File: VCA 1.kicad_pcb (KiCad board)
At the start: 2 copper layers, 185.7 x 142.5 mm, 46 parts, among them J1 Eurorack 2x8hs, J10 IN3, J11 IN4, J12 IN5, J13 OUT1, J14 OUT2, J15 OUT3, J16 OUT4, J2 LED 1x2s, J3 IN 1x6s, J4 OUT 1x4s, J5 LED 1x2h, J6 IN 1x6h, J7 OUT 1x4h, J8 IN1, J9 IN2, U1 TL074

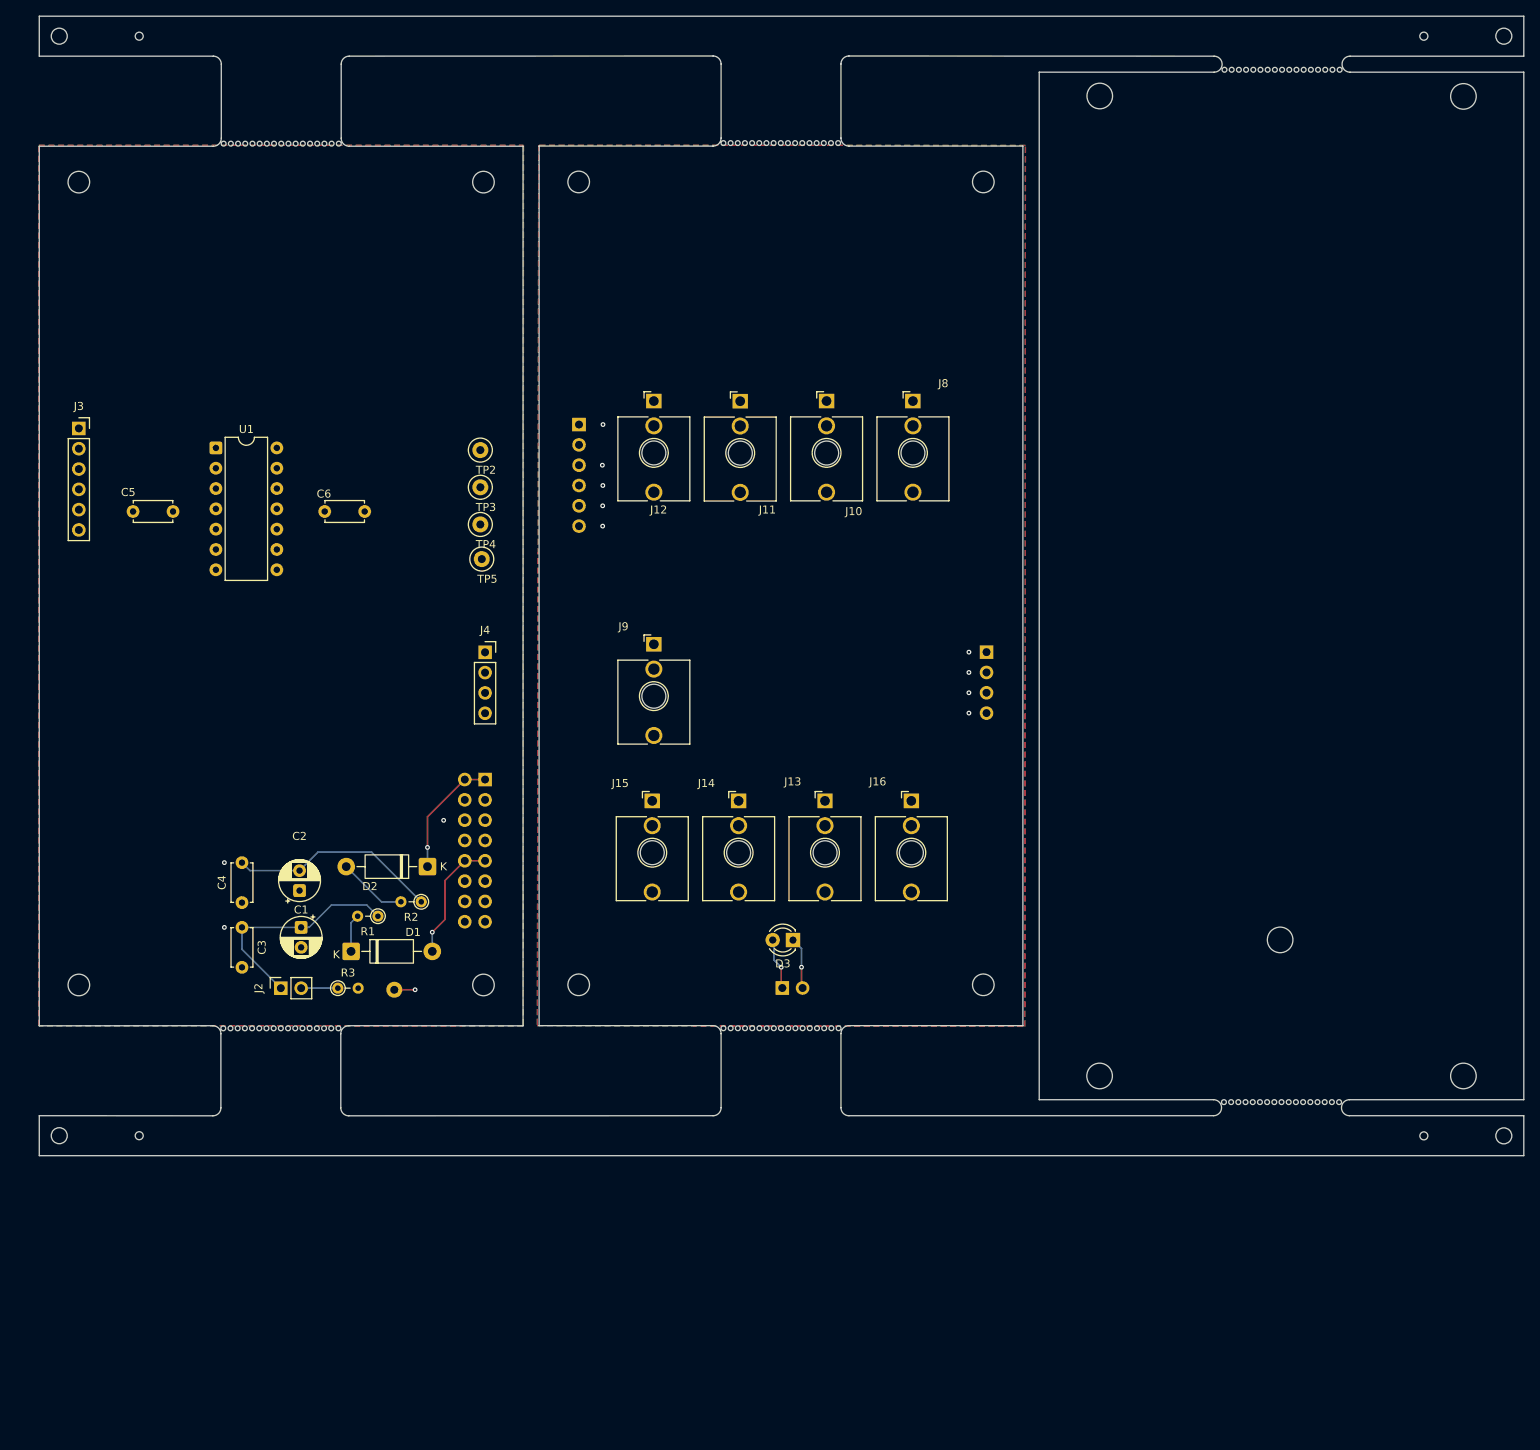
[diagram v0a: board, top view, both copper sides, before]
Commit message: Started on the PCB layout
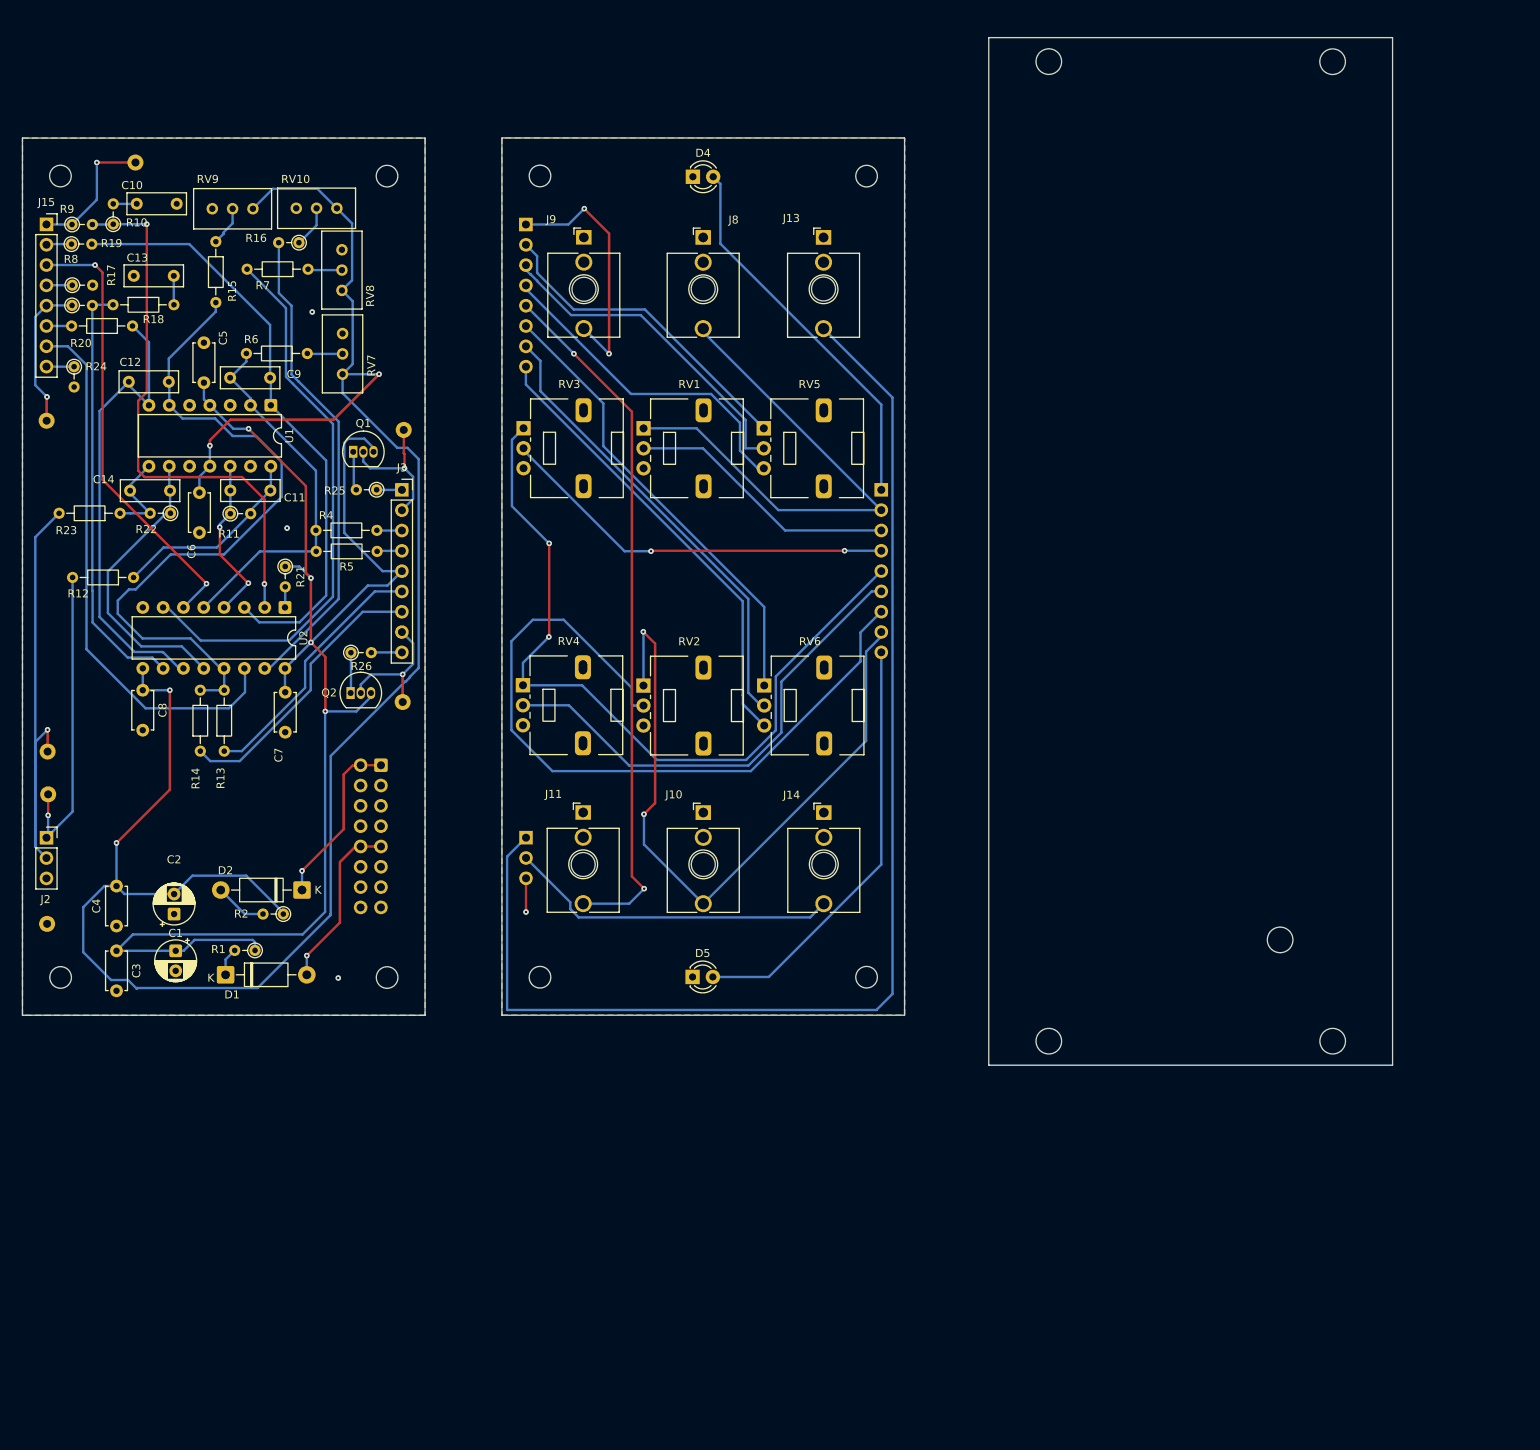
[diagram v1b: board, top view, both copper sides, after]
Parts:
- removed D3: LED, LED_THT:LED_D3.0mm_FlatTop
- removed J16: OUT4, Connector_Audio:Jack_3.5mm_QingPu_WQP-PJ398SM_Vertical_CircularHoles
- removed J4: OUT 1x4s, Connector_PinSocket_2.54mm:PinSocket_1x04_P2.54mm_Vertical
- removed J7: OUT 1x4h, Connector_PinHeader_2.54mm:PinHeader_1x04_P2.54mm_Vertical
- removed R3: 470R/520R, Resistor_THT:R_Axial_DIN0204_L3.6mm_D1.6mm_P2.54mm_Vertical
- added C10: 470pF f, Capacitor_THT:C_Rect_L7.2mm_W2.5mm_P5.00mm, F.Cu at (39.3, 38.1)
- added C11: 100pF f, Capacitor_THT:C_Rect_L7.2mm_W2.5mm_P5.00mm, F.Cu at (51.0, 74.0)
- added C12: 100pF f, Capacitor_THT:C_Rect_L7.2mm_W2.5mm_P5.00mm, F.Cu at (43.3, 60.4)
- added C13: 470pF f, Capacitor_THT:C_Rect_L7.2mm_W2.5mm_P5.00mm, F.Cu at (43.9, 47.2)
- added C14: 100pF f, Capacitor_THT:C_Rect_L7.2mm_W2.5mm_P5.00mm, F.Cu at (43.5, 74.0)
- added C7: 1μF c, Capacitor_THT:C_Disc_D4.7mm_W2.5mm_P5.00mm, F.Cu at (57.9, 99.2)
- added C8: 1μF c, Capacitor_THT:C_Disc_D4.7mm_W2.5mm_P5.00mm, F.Cu at (40.0, 99.0)
- added C9: 100pF f, Capacitor_THT:C_Rect_L7.2mm_W2.5mm_P5.00mm, F.Cu at (51.0, 59.9)
- added D4: LED, LED_THT:LED_D3.0mm_FlatTop, F.Cu at (108.8, 34.8)
- added D5: LED, LED_THT:LED_D3.0mm_FlatTop, F.Cu at (108.8, 134.8)
- added Q1: 2N3904, Package_TO_SOT_THT:TO-92_Inline, F.Cu at (66.4, 69.2)
- added Q2: 2N3904, Package_TO_SOT_THT:TO-92_Inline, F.Cu at (66.0, 99.3)
- added R10: 470R, Resistor_THT:R_Axial_DIN0204_L3.6mm_D1.6mm_P2.54mm_Vertical, F.Cu at (36.4, 40.7)
- added R11: 10K, Resistor_THT:R_Axial_DIN0204_L3.6mm_D1.6mm_P2.54mm_Vertical, F.Cu at (51.0, 76.9)
- added R12: 470R, Resistor_THT:R_Axial_DIN0204_L3.6mm_D1.6mm_P7.62mm_Horizontal, F.Cu at (38.9, 84.9)
- added R13: 10K, Resistor_THT:R_Axial_DIN0204_L3.6mm_D1.6mm_P7.62mm_Horizontal, F.Cu at (50.2, 106.6)
- added R14: 10K, Resistor_THT:R_Axial_DIN0204_L3.6mm_D1.6mm_P7.62mm_Horizontal, F.Cu at (47.2, 106.6)
- added R15: 33K, Resistor_THT:R_Axial_DIN0204_L3.6mm_D1.6mm_P7.62mm_Horizontal, F.Cu at (49.2, 42.9)
- added R16: 22K, Resistor_THT:R_Axial_DIN0204_L3.6mm_D1.6mm_P2.54mm_Vertical, F.Cu at (59.6, 43.0)
- added R17: 150K, Resistor_THT:R_Axial_DIN0204_L3.6mm_D1.6mm_P2.54mm_Vertical, F.Cu at (31.2, 50.9)
- added R18: 470R, Resistor_THT:R_Axial_DIN0204_L3.6mm_D1.6mm_P7.62mm_Horizontal, F.Cu at (36.3, 50.8)
- added R19: 10K, Resistor_THT:R_Axial_DIN0204_L3.6mm_D1.6mm_P2.54mm_Vertical, F.Cu at (31.1, 43.2)
- added R20: 10K, Resistor_THT:R_Axial_DIN0204_L3.6mm_D1.6mm_P7.62mm_Horizontal, F.Cu at (38.8, 53.4)
- added R21: 7K5, Resistor_THT:R_Axial_DIN0204_L3.6mm_D1.6mm_P2.54mm_Vertical, F.Cu at (57.9, 83.5)
- added R22: 10K, Resistor_THT:R_Axial_DIN0204_L3.6mm_D1.6mm_P2.54mm_Vertical, F.Cu at (43.5, 76.8)
- added R23: 470R, Resistor_THT:R_Axial_DIN0204_L3.6mm_D1.6mm_P7.62mm_Horizontal, F.Cu at (37.2, 76.9)
- added R24: 2K2, Resistor_THT:R_Axial_DIN0204_L3.6mm_D1.6mm_P2.54mm_Vertical, F.Cu at (31.5, 58.5)
- added R25: 470R, Resistor_THT:R_Axial_DIN0204_L3.6mm_D1.6mm_P2.54mm_Vertical, F.Cu at (69.3, 73.9)
- added R26: 470R, Resistor_THT:R_Axial_DIN0204_L3.6mm_D1.6mm_P2.54mm_Vertical, F.Cu at (66.1, 94.3)
- added R4: 10K, Resistor_THT:R_Axial_DIN0204_L3.6mm_D1.6mm_P7.62mm_Horizontal, F.Cu at (69.3, 79.0)
- added R5: 10K, Resistor_THT:R_Axial_DIN0204_L3.6mm_D1.6mm_P7.62mm_Horizontal, F.Cu at (69.3, 81.6)
- added R6: 33K, Resistor_THT:R_Axial_DIN0204_L3.6mm_D1.6mm_P7.62mm_Horizontal, F.Cu at (60.6, 56.9)
- added R7: 22K, Resistor_THT:R_Axial_DIN0204_L3.6mm_D1.6mm_P7.62mm_Horizontal, F.Cu at (60.7, 46.3)
- added R8: 2K2, Resistor_THT:R_Axial_DIN0204_L3.6mm_D1.6mm_P2.54mm_Vertical, F.Cu at (31.2, 48.3)
- added R9: 150K, Resistor_THT:R_Axial_DIN0204_L3.6mm_D1.6mm_P2.54mm_Vertical, F.Cu at (31.2, 40.7)
- added RV1: 10K B, Potentiometer_THT:Potentiometer_Alps_RK09L_Single_Vertical, F.Cu at (102.7, 66.2)
- added RV10: 10K, Potentiometer_THT:Potentiometer_Bourns_3296W_Vertical, F.Cu at (64.3, 38.7)
- added RV2: 10K B, Potentiometer_THT:Potentiometer_Alps_RK09L_Single_Vertical, F.Cu at (102.7, 98.4)
- added RV3: 50K B, Potentiometer_THT:Potentiometer_Alps_RK09L_Single_Vertical, F.Cu at (87.7, 66.2)
- added RV4: 50K B, Potentiometer_THT:Potentiometer_Alps_RK09L_Single_Vertical, F.Cu at (87.6, 98.4)
- added RV5: 10K B, Potentiometer_THT:Potentiometer_Alps_RK09L_Single_Vertical, F.Cu at (117.7, 66.2)
- added RV6: 10K B, Potentiometer_THT:Potentiometer_Alps_RK09L_Single_Vertical, F.Cu at (117.8, 98.4)
- added RV7: 100K, Potentiometer_THT:Potentiometer_Bourns_3296W_Vertical, F.Cu at (65.0, 59.5)
- added RV8: 10K, Potentiometer_THT:Potentiometer_Bourns_3296W_Vertical, F.Cu at (65.0, 49.0)
- added RV9: 100K, Potentiometer_THT:Potentiometer_Bourns_3296W_Vertical, F.Cu at (53.8, 38.8)
- added TP6: CV1, TestPoint:TestPoint_Loop_D2.50mm_Drill1.0mm, B.Cu at (72.7, 66.4)
- added TP7: CV2, TestPoint:TestPoint_Loop_D2.50mm_Drill1.0mm, B.Cu at (72.5, 100.5)
- added U2: AS2164, Package_DIP:DIP-16_W7.62mm, F.Cu at (57.8, 88.6)
- J1: footprint Connector_PinHeader_2.54mm:PinHeader_2x08_P2.54mm_Vertical -> Connector_IDC:IDC-Header_2x08_P2.54mm_Vertical
- J10: value IN3 -> CV2
- J11: value IN4 -> IN2
- J12: value IN5 -> IN 1x8h; footprint Connector_Audio:Jack_3.5mm_QingPu_WQP-PJ398SM_Vertical_CircularHoles -> Connector_PinHeader_2.54mm:PinHeader_1x08_P2.54mm_Vertical; moved to B.Cu
- J15: value OUT3 -> IN 1x8s; footprint Connector_Audio:Jack_3.5mm_QingPu_WQP-PJ398SM_Vertical_CircularHoles -> Connector_PinSocket_2.54mm:PinSocket_1x08_P2.54mm_Vertical
- J2: value LED 1x2s -> OUT 1x3s; footprint Connector_PinSocket_2.54mm:PinSocket_1x02_P2.54mm_Vertical -> Connector_PinSocket_2.54mm:PinSocket_1x03_P2.54mm_Vertical
- J3: value IN 1x6s -> CV 1x9s; footprint Connector_PinSocket_2.54mm:PinSocket_1x06_P2.54mm_Vertical -> Connector_PinSocket_2.54mm:PinSocket_1x09_P2.54mm_Vertical
- J5: value LED 1x2h -> CV 1x9h; footprint Connector_PinHeader_2.54mm:PinHeader_1x02_P2.54mm_Vertical -> Connector_PinHeader_2.54mm:PinHeader_1x09_P2.54mm_Vertical
- J6: value IN 1x6h -> OUT 1x3h; footprint Connector_PinHeader_2.54mm:PinHeader_1x06_P2.54mm_Vertical -> Connector_PinHeader_2.54mm:PinHeader_1x03_P2.54mm_Vertical
- J8: value IN1 -> CV1
- J9: value IN2 -> IN1
- TP2, TP3: moved to B.Cu
- TP4: value OUT3 -> IN1; moved to B.Cu
- TP5: value OUT4 -> IN2; moved to B.Cu
- moved J15 104.6 mm to (28.0, 40.7)
- moved J13 70.5 mm to (125.2, 42.4)
- moved TP2 69.1 mm to (28.2, 112.0), turned to 180 degrees
- moved J5 63.5 mm to (132.4, 73.9), turned to 180 degrees
- moved TP3 63.4 mm to (28.1, 106.7), turned to 180 degrees
- moved TP4 62.5 mm to (39.1, 33.0), turned to 180 degrees
- moved TP5 57.1 mm to (28.0, 65.3), turned to 180 degrees
- moved J11 55.1 mm to (95.1, 114.3)
- moved J10 53.7 mm to (110.1, 114.3)
- moved J6 52.1 mm to (88.0, 117.4)
- moved J9 51.6 mm to (95.2, 42.4)
- moved TP1 44.2 mm to (28.1, 128.2)
- moved J3 41.1 mm to (72.5, 73.9)
- moved J2 34.8 mm to (28.0, 117.4), turned to 0 degrees
- moved J8 33.3 mm to (110.1, 42.4)
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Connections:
- J10 pad T: Net-(J6-Pin_3) -> Net-(J5-Pin_8)
- J11 pad T: Net-(J6-Pin_4) -> Net-(J12-Pin_5)
- J13 pad T: Net-(J7-Pin_1) -> Net-(J6-Pin_1)
- J14 pad T: Net-(J7-Pin_2) -> Net-(J6-Pin_2)
- J2 pad 1: +12V -> Net-(J2-Pin_1)
- J3 pad 1: unconnected-(J3-Pin_1-Pad1) -> Net-(J3-Pin_1)
- J3 pad 2: unconnected-(J3-Pin_2-Pad2) -> Net-(J3-Pin_2)
- J3 pad 3: unconnected-(J3-Pin_3-Pad3) -> Net-(J3-Pin_3)
- J3 pad 4: unconnected-(J3-Pin_4-Pad4) -> Net-(J3-Pin_4)
- J3 pad 5: unconnected-(J3-Pin_5-Pad5) -> +12V
- J3 pad 6: GND -> Net-(J3-Pin_6)
- J5 pad 2: Net-(D3-K) -> Net-(J5-Pin_2)
- J6 pad 3: Net-(J6-Pin_3) -> GND
- J8 pad T: Net-(J6-Pin_1) -> Net-(J5-Pin_2)
- J9 pad T: Net-(J6-Pin_2) -> Net-(J12-Pin_1)
- TP2 pad 1: Net-(J4-Pin_1) -> Net-(J2-Pin_1)
- TP3 pad 1: Net-(J4-Pin_2) -> Net-(J2-Pin_2)
- TP4 pad 1: Net-(J4-Pin_3) -> Net-(J15-Pin_1)
- TP5 pad 1: Net-(J4-Pin_4) -> Net-(J15-Pin_5)
- U1 pad 1: (no net) -> Net-(U2-VC1)
- U1 pad 10: (no net) -> GND
- U1 pad 12: (no net) -> Net-(U1D-+)
- U1 pad 13: (no net) -> GND
- U1 pad 14: (no net) -> Net-(C11-Pad2)
- U1 pad 2: (no net) -> Net-(U1A--)
- U1 pad 3: (no net) -> GND
- U1 pad 5: (no net) -> GND
- U1 pad 6: (no net) -> Net-(U1B--)
- U1 pad 7: (no net) -> Net-(U2-VC3)
- U1 pad 8: (no net) -> Net-(C14-Pad2)
- U1 pad 9: (no net) -> Net-(U1C--)
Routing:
- net -12V: track 41.7 -> 275.8 mm, vias 2 -> 5
- net Net-(J6-Pin_1): track 0.00 -> 158.3 mm, vias 1 -> 0
- net +12V: track 44.3 -> 201.2 mm, vias 2 -> 5
- net Net-(J5-Pin_5): track 0.00 -> 98.5 mm, vias 0 -> 2
- net Net-(J5-Pin_7): track 0.00 -> 93.1 mm
- net Net-(J5-Pin_8): track 0.00 -> 88.2 mm, vias 0 -> 2
- net Net-(J12-Pin_5): track 0.00 -> 87.4 mm, vias 0 -> 2
- net Net-(U1B--): track 0.00 -> 86.0 mm
- net Net-(U2-VC1): track 0.00 -> 75.6 mm
- net Net-(U2-I_IN2): track 0.00 -> 70.6 mm
- net Net-(U2-I_IN1): track 0.00 -> 68.9 mm, vias 0 -> 2
- net Net-(J15-Pin_7): track 0.00 -> 68.3 mm
- net Net-(J5-Pin_2): track 0.00 -> 65.9 mm
- net Net-(J5-Pin_6): track 0.00 -> 60.7 mm
- net Net-(U2-I_IN4): track 0.00 -> 60.5 mm
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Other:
- board size 185.7 x 142.5 mm -> 171.3 x 128.5 mm

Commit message: PCB passes EDC and panel cutouts done
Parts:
- Q1, Q2: footprint Package_TO_SOT_THT:TO-92_Inline -> Package_TO_SOT_THT:TO-92_Inline_Wide
- moved Q2 1.38 mm to (64.7, 99.3)
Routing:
- net -12V: track 275.8 -> 282.4 mm
- net +12V: track 201.2 -> 205.2 mm
- net Net-(J3-Pin_2): track 17.8 -> 16.3 mm
- net Net-(Q2-E): track 5.07 -> 5.65 mm
- net Net-(J3-Pin_8): track 16.7 -> 16.2 mm
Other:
- outline, holes or cut-outs redrawn
- board text added: "V 1.0"

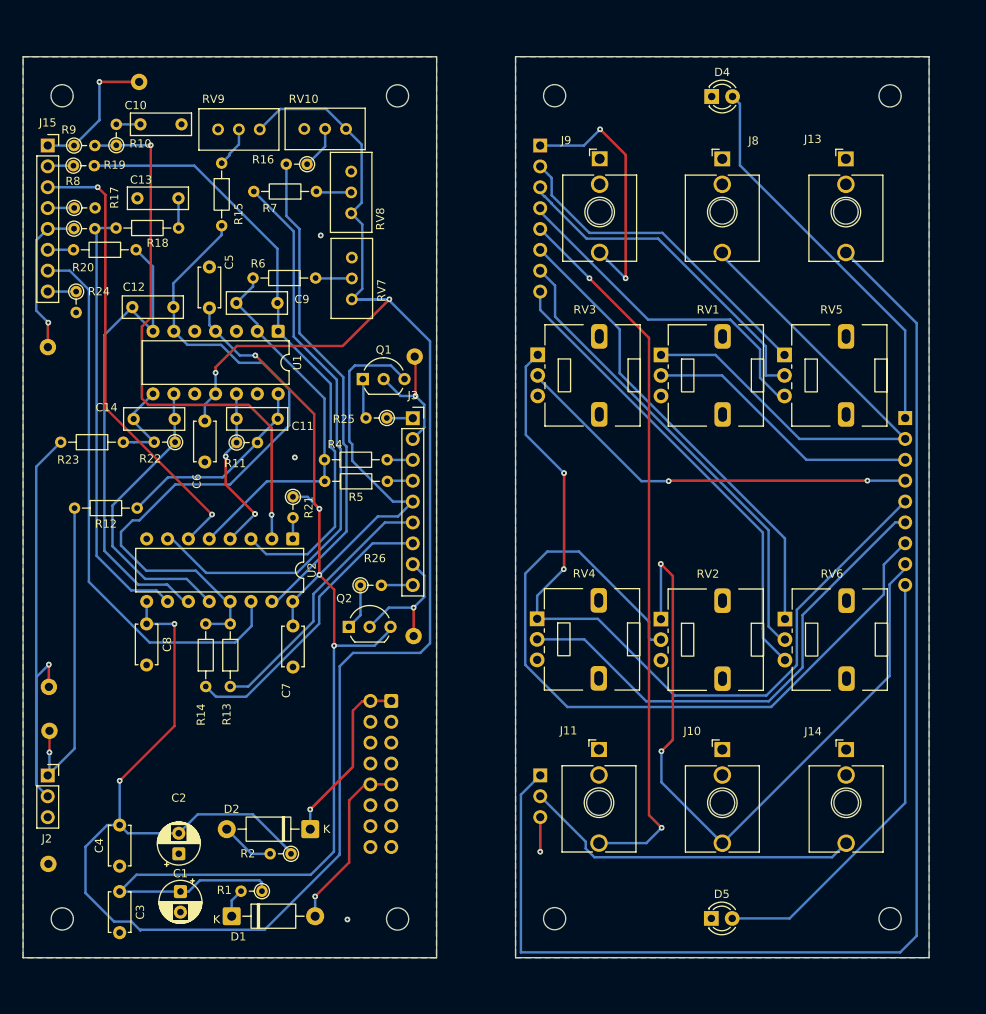
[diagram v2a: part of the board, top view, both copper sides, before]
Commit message: Connected ground islands
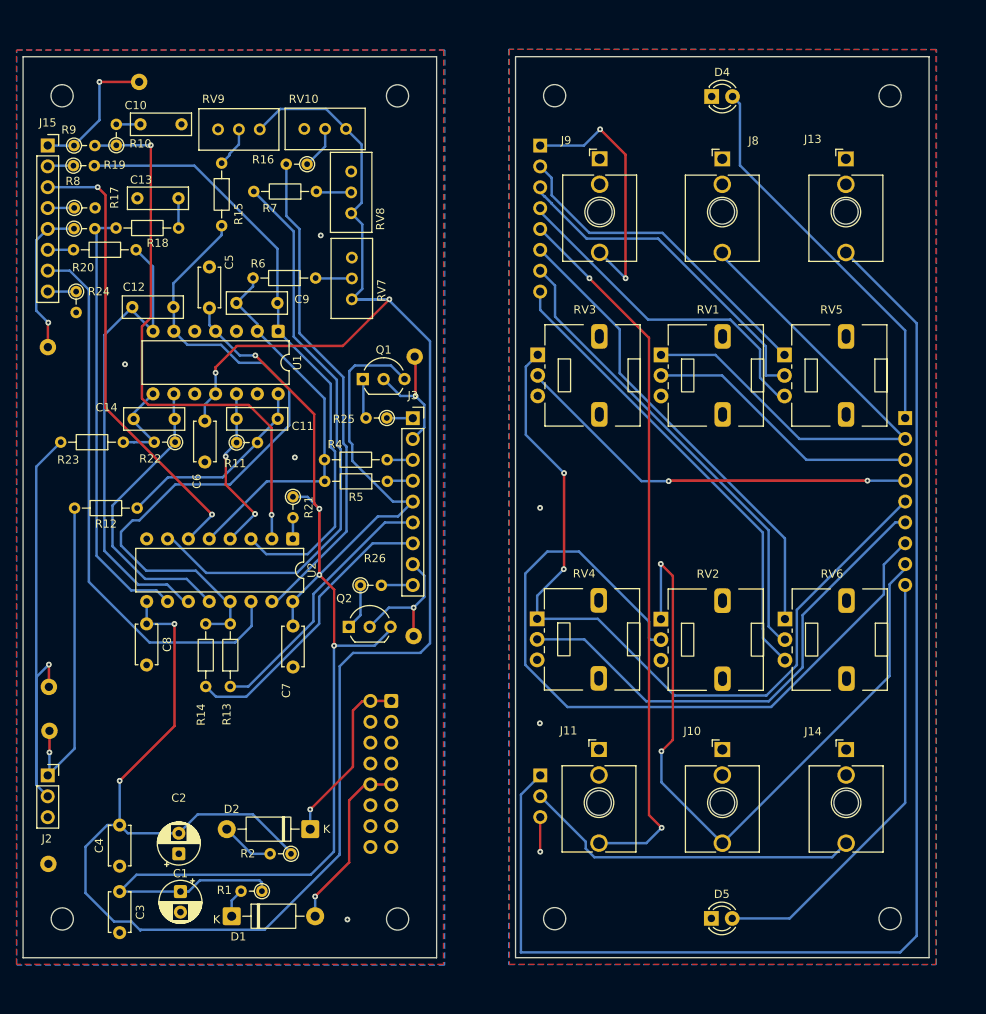
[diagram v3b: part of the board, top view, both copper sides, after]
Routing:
- net GND: vias 4 -> 7
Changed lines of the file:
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@@
 	)
 	(via
+		(at 87.95 84.85)
+		(size 0.7)
+		(drill 0.3)
+		(layers "F.Cu" "B.Cu")
+		(free yes)
+		(net "GND")
+	)
+	(via
 		(at 61.24 51.68)
 		(size 0.7)
@@
 	)
 	(via
+		(at 37.41 67.37)
+		(size 0.7)
+		(drill 0.3)
+		(layers "F.Cu" "B.Cu")
+		(free yes)
+		(net "GND")
+	)
+	(via
+		(at 87.92 111.08)
+		(size 0.7)
+		(drill 0.3)
+		(layers "F.Cu" "B.Cu")
+		(free yes)
+		(net "GND")
+	)
+	(via
 		(at 64.49 134.97)
 		(size 0.7)
@@
 		(polygon
 			(pts
-				(xy 25 29.93) (xy 75.350572 29.93) (xy 75.328415 139.635152) (xy 25 139.624988)
+				(xy 24.19 29.11) (xy 76.201244 29.11) (xy 76.178758 140.435252) (xy 24.19 140.424752)
 			)
 		)
@@
 		(polygon
 			(pts
-				(xy 84.960282 29.917057) (xy 84.963703 139.613692) (xy 135.314827 139.62631) (xy 135.342312 29.949555)
+				(xy 84.20825 29.023248) (xy 84.211724 140.423504) (xy 136.126156 140.436513) (xy 136.154068 29.056754)
 			)
 		)
@@
 		(polygon
 			(pts
-				(xy 25 29.93) (xy 75.35 29.93) (xy 75.327842 139.635152) (xy 25 139.624988)
+				(xy 24.23 29.1) (xy 76.351246 29.1) (xy 76.32874 140.525262) (xy 24.23 140.51474)
 			)
 		)
@@
 		(polygon
 			(pts
-				(xy 84.965854 29.924414) (xy 84.967964 139.61364) (xy 135.314599 139.626362) (xy 135.342312 29.949549)
+				(xy 84.118938 29.017002) (xy 84.121082 140.453424) (xy 136.185794 140.46658) (xy 136.213948 29.042996)
 			)
 		)
